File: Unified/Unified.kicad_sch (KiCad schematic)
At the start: 56 parts, among them J1 USB_C_Receptacle_USB2.0_16P, J10 JST_switch_1, J11 JST_switch_2, J12 Conn_touch_1, J13 Conn_touch_2, J14 Bat_pos_sel, J15 Bat_neg_sel, J16 JST_header, J2 JST_battery, J3 JST_header, J4 JST_speaker, J5 JST_debug_swd, J6 JST_debug_serial, J7 Conn_speaker_sd, J8 Conn_speaker_gain, J9 Conn_speaker_gnd, Q1 AO3401A, Q2 AO3400A, SW1 SW_power, U1 MCP73831-2-OT, U2 MAX98357A

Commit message: Add LEDs to unified PCB, currently routing
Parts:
- removed J16: JST_header, Connector_JST:JST_SH_BM04B-SRSS-TB_1x04-1MP_P1.00mm_Vertical, symbol Connector_Generic:Conn_01x04
- renumbered D9 to D10, D10 to D11, D11 to D12, D12 to D13, D13 to D14, D14 to D15, D15 to D16, D16 to D9
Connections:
- no-connect marks 4 -> 3
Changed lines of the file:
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@@
 		(at 29.21 67.31)
 	)
-	(no_connect
-		(at 33.02 199.39)
-	)
 	(wire
 		(pts
@@
 	(wire
 		(pts
-			(xy 33.02 191.77) (xy 36.83 191.77)
-		)
-		(stroke
-			(width 0)
-			(type default)
-		)
-	)
-	(wire
-		(pts
 			(xy 167.64 113.03) (xy 167.64 116.84)
 		)
@@
 	(wire
 		(pts
-			(xy 33.02 196.85) (xy 36.83 196.85)
-		)
-		(stroke
-			(width 0)
-			(type default)
-		)
-	)
-	(wire
-		(pts
 			(xy 311.15 132.08) (xy 317.5 132.08)
 		)
@@
 	(wire
 		(pts
-			(xy 33.02 199.39) (xy 36.83 199.39)
-		)
-		(stroke
-			(width 0)
-			(type default)
-		)
-	)
-	(wire
-		(pts
 			(xy 142.24 35.56) (xy 142.24 45.72)
 		)
@@
 	(wire
 		(pts
-			(xy 33.02 194.31) (xy 36.83 194.31)
-		)
-		(stroke
-			(width 0)
-			(type default)
-		)
-	)
-	(wire
-		(pts
 			(xy 99.06 168.91) (xy 102.87 168.91)
 		)
@@
 		)
 	)
-	(label "BAT_-"
-		(at 33.02 194.31 180)
-		(effects
-			(font
-				(size 1.27 1.27)
-			)
-			(justify right bottom)
-		)
-	)
 	(label "SPEAKER_LRC"
 		(at 90.17 152.4 180)
@@
 		)
 	)
-	(label "WS2812B_VS"
-		(at 33.02 191.77 180)
-		(effects
-			(font
-				(size 1.27 1.27)
-			)
-			(justify right bottom)
-		)
-	)
 	(label "SPEAKER_+"
 		(at 242.57 19.05 180)
@@
 		)
 	)
-	(label "WS2812B_DIN"
-		(at 33.02 196.85 180)
-		(effects
-			(font
-				(size 1.27 1.27)
-			)
-			(justify right bottom)
-		)
-	)
 	(symbol
 		(lib_id "LED:WS2812B")
@@
 		(dnp no)
 		(fields_autoplaced yes)
-		(property "Reference" "D14"
+		(property "Reference" "D15"
 			(at 212.09 223.4498 0)
 			(show_name no)
@@
 			(project "Unified"
 				(path "/86209ff5-e3e5-4edf-9087-a19295ca511e"
-					(reference "D14")
+					(reference "D15")
 					(unit 1)
 				)
@@
 		(dnp no)
 		(fields_autoplaced yes)
-		(property "Reference" "D15"
+		(property "Reference" "D16"
 			(at 237.49 223.4498 0)
 			(show_name no)
@@
 			(project "Unified"
 				(path "/86209ff5-e3e5-4edf-9087-a19295ca511e"
-					(reference "D15")
+					(reference "D16")
 					(unit 1)
 				)
@@
 		(dnp no)
 		(fields_autoplaced yes)
-		(property "Reference" "D13"
+		(property "Reference" "D14"
 			(at 186.69 223.4498 0)
 			(show_name no)
@@
 			(project "Unified"
 				(path "/86209ff5-e3e5-4edf-9087-a19295ca511e"
-					(reference "D13")
+					(reference "D14")
 					(unit 1)
 				)
@@
 	)
 	(symbol
-		(lib_id "Connector_Generic:Conn_01x04")
-		(at 41.91 194.31 0)
-		(unit 1)
-		(body_style 1)
-		(exclude_from_sim no)
-		(in_bom yes)
-		(on_board yes)
-		(in_pos_files yes)
-		(dnp no)
-		(property "Reference" "J16"
-			(at 45.212 192.532 0)
-			(show_name no)
-			(do_not_autoplace no)
-			(effects
-				(font
-					(size 1.27 1.27)
-				)
-			)
-		)
-		(property "Value" "JST_header"
-			(at 49.53 194.564 0)
-			(show_name no)
-			(do_not_autoplace no)
-			(effects
-				(font
-					(size 1.27 1.27)
-				)
-			)
-		)
-		(property "Footprint" "Connector_JST:JST_SH_BM04B-SRSS-TB_1x04-1MP_P1.00mm_Vertical"
-			(at 41.91 194.31 0)
-			(hide yes)
-			(show_name no)
-			(do_not_autoplace no)
-			(effects
-				(font
-					(size 1.27 1.27)
-				)
-			)
-		)
-		(property "Datasheet" ""
-			(at 41.91 194.31 0)
-			(hide yes)
-			(show_name no)
-			(do_not_autoplace no)
-			(effects
-				(font
-					(size 1.27 1.27)
-				)
-			)
-		)
-		(property "Description" "Generic connector, single row, 01x04, script generated (kicad-library-utils/schlib/autogen/connector/)"
-			(at 41.91 194.31 0)
-			(hide yes)
-			(show_name no)
-			(do_not_autoplace no)
-			(effects
-				(font
-					(size 1.27 1.27)
-				)
-			)
-		)
-		(pin "3"
-		)
-		(pin "1"
-		)
-		(pin "2"
-		)
-		(pin "4"
-		)
-		(instances
-			(project "Unified"
-				(path "/86209ff5-e3e5-4edf-9087-a19295ca511e"
-					(reference "J16")
-					(unit 1)
-				)
-			)
-		)
-	)
-	(symbol
 		(lib_id "LED:WS2812B")
 		(at 72.39 229.87 0)
@@
 		(dnp no)
 		(fields_autoplaced yes)
-		(property "Reference" "D9"
+		(property "Reference" "D10"
 			(at 83.82 223.4498 0)
 			(show_name no)
@@
 			(project "Unified"
 				(path "/86209ff5-e3e5-4edf-9087-a19295ca511e"
-					(reference "D9")
+					(reference "D10")
 					(unit 1)
 				)
@@
 		(dnp no)
 		(fields_autoplaced yes)
-		(property "Reference" "D16"
+		(property "Reference" "D9"
 			(at 262.89 192.9698 0)
 			(show_name no)
@@
 			(project "Unified"
 				(path "/86209ff5-e3e5-4edf-9087-a19295ca511e"
-					(reference "D16")
+					(reference "D9")
 					(unit 1)
 				)
@@
 		(dnp no)
 		(fields_autoplaced yes)
-		(property "Reference" "D11"
+		(property "Reference" "D12"
 			(at 135.89 223.4498 0)
 			(show_name no)
@@
 			(project "Unified"
 				(path "/86209ff5-e3e5-4edf-9087-a19295ca511e"
-					(reference "D11")
+					(reference "D12")
 					(unit 1)
 				)
@@
 		(dnp no)
 		(fields_autoplaced yes)
-		(property "Reference" "D10"
+		(property "Reference" "D11"
 			(at 110.49 223.4498 0)
 			(show_name no)
@@
 			(project "Unified"
 				(path "/86209ff5-e3e5-4edf-9087-a19295ca511e"
-					(reference "D10")
+					(reference "D11")
 					(unit 1)
 				)
@@
 		(dnp no)
 		(fields_autoplaced yes)
-		(property "Reference" "D12"
+		(property "Reference" "D13"
 			(at 161.29 223.4498 0)
 			(show_name no)
@@
 			(project "Unified"
 				(path "/86209ff5-e3e5-4edf-9087-a19295ca511e"
-					(reference "D12")
+					(reference "D13")
 					(unit 1)
 				)

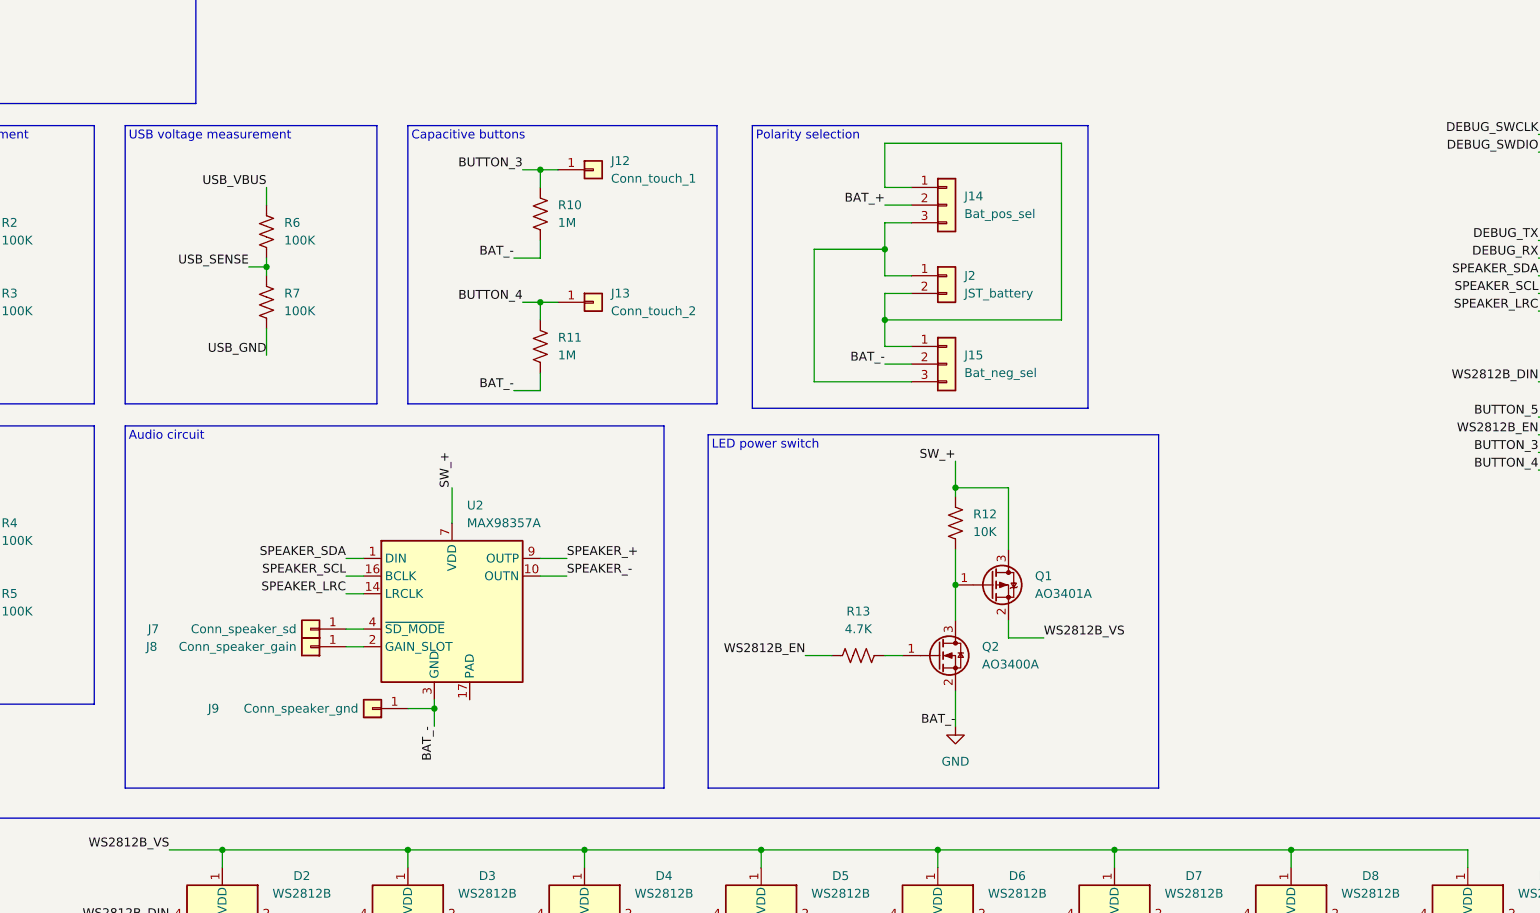
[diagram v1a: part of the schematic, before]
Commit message: Re-arrange for pin header for speaker
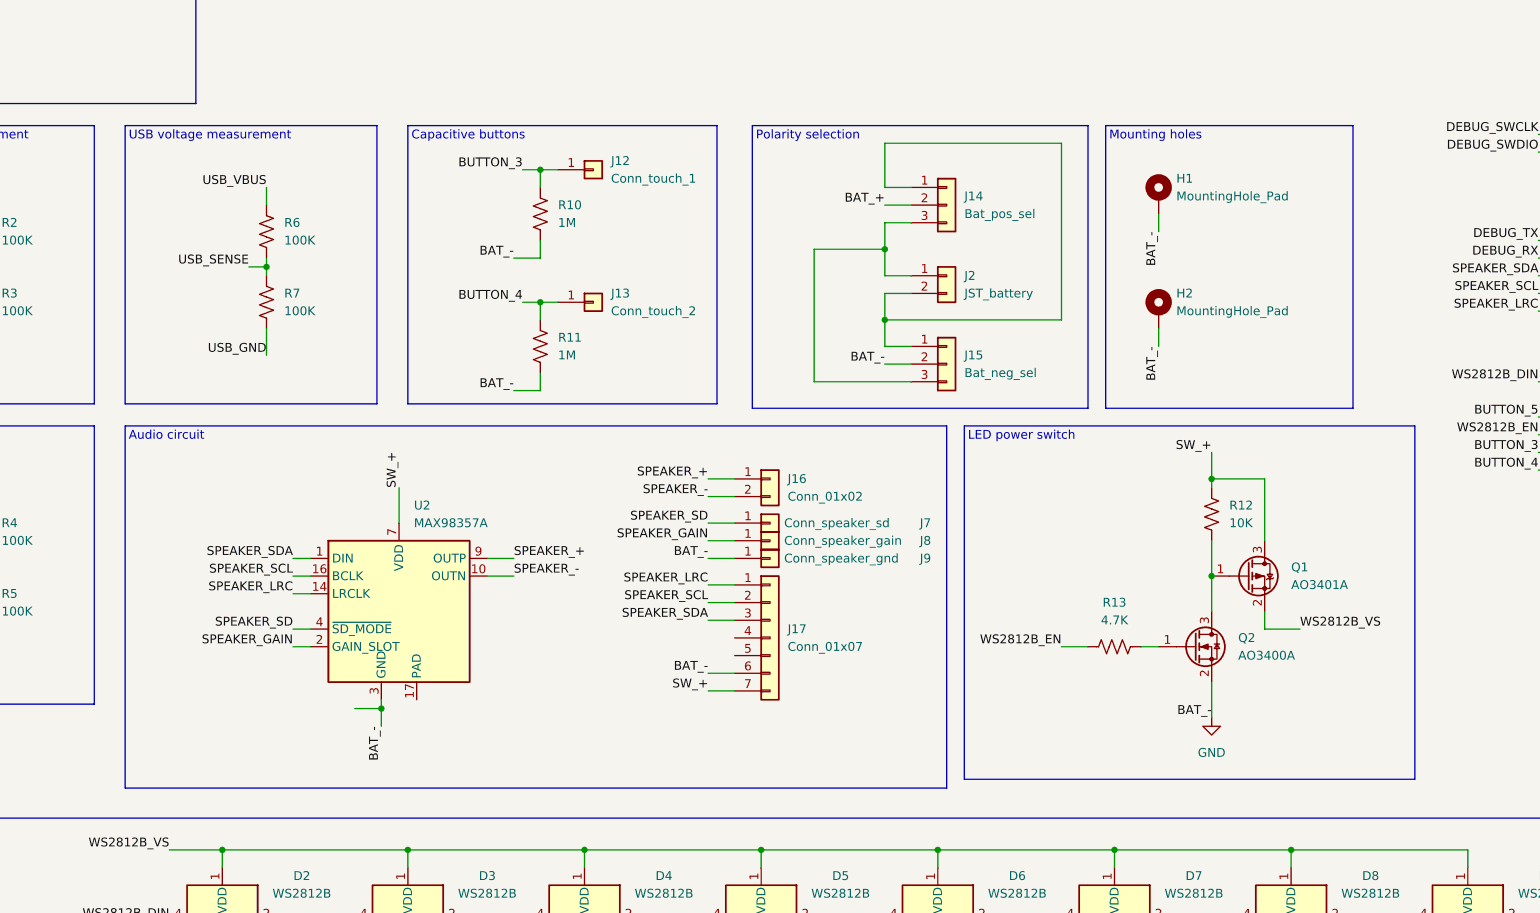
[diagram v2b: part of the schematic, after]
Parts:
- added H1, H2: MountingHole_Pad, MountingHole:MountingHole_4.3mm_M4_ISO7380_Pad, symbol Mechanical:MountingHole_Pad
- added J16: Conn_01x02, Connector_PinHeader_2.54mm:PinHeader_1x02_P2.54mm_Vertical, symbol Connector_Generic:Conn_01x02
- added J17: Conn_01x07, Connector_PinSocket_2.54mm:PinSocket_1x07_P2.54mm_Vertical, symbol Connector_Generic:Conn_01x07
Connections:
- net GND: now also H1.1, H2.1, J17.6 (Pin_6)
- net SPEAKER_+: now also J16.1 (Pin_1)
- net SPEAKER_-: now also J16.2 (Pin_2)
- net SPEAKER_LRC: now also J17.1 (Pin_1)
- net SPEAKER_SCL: now also J17.2 (Pin_2)
- net SPEAKER_SDA: now also J17.3 (Pin_3)
- net SW_+: now also J17.7 (Pin_7)
- net SPEAKER_GAIN: now reaches J8.1 (Pin_1), U2.2 (GAIN_SLOT)
- net SPEAKER_SD: now reaches J7.1 (Pin_1), U2.4 (~{SD_MODE})
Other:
- note added: "Mounting holes"
- moved on the sheet: Q1, Q2, R12, R13, U2

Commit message: Finalize routing, bump to V5
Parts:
- H1, H2: footprint MountingHole:MountingHole_4.3mm_M4_ISO7380_Pad -> MountingHole:MountingHole_2.2mm_M2_ISO7380_Pad
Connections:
- no-connect marks 3 -> 5
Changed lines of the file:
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@@
 	(paper "USLedger")
 	(title_block
-		(rev "V4")
+		(rev "V5")
 	)
 	(rectangle
@@
 	)
 	(junction
-		(at 95.25 168.91)
-		(diameter 0)
-		(color 0 0 0 0)
-	)
-	(junction
 		(at 99.06 219.71)
 		(diameter 0)
@@
 	)
 	(no_connect
+		(at 146.05 158.75)
+	)
+	(no_connect
 		(at 29.21 67.31)
 	)
+	(no_connect
+		(at 146.05 161.29)
+	)
 	(wire
 		(pts
@@
 	(wire
 		(pts
-			(xy 95.25 167.64) (xy 95.25 168.91)
-		)
-		(stroke
-			(width 0)
-			(type default)
-		)
-	)
-	(wire
-		(pts
 			(xy 200.66 189.23) (xy 226.06 189.23)
 		)
@@
 	(wire
 		(pts
-			(xy 95.25 168.91) (xy 95.25 171.45)
+			(xy 95.25 167.64) (xy 95.25 171.45)
 		)
 		(stroke
@@
 	(wire
 		(pts
-			(xy 91.44 168.91) (xy 95.25 168.91)
-		)
-		(stroke
-			(width 0)
-			(type default)
-		)
-	)
-	(wire
-		(pts
 			(xy 261.62 88.9) (xy 265.43 88.9)
 		)
@@
 			)
 		)
-		(property "Footprint" "MountingHole:MountingHole_4.3mm_M4_ISO7380_Pad"
+		(property "Footprint" "MountingHole:MountingHole_2.2mm_M2_ISO7380_Pad"
 			(at 207.01 95.25 0)
 			(hide yes)
@@
 			)
 		)
-		(property "Footprint" "MountingHole:MountingHole_4.3mm_M4_ISO7380_Pad"
+		(property "Footprint" "MountingHole:MountingHole_2.2mm_M2_ISO7380_Pad"
 			(at 207.01 111.76 0)
 			(hide yes)

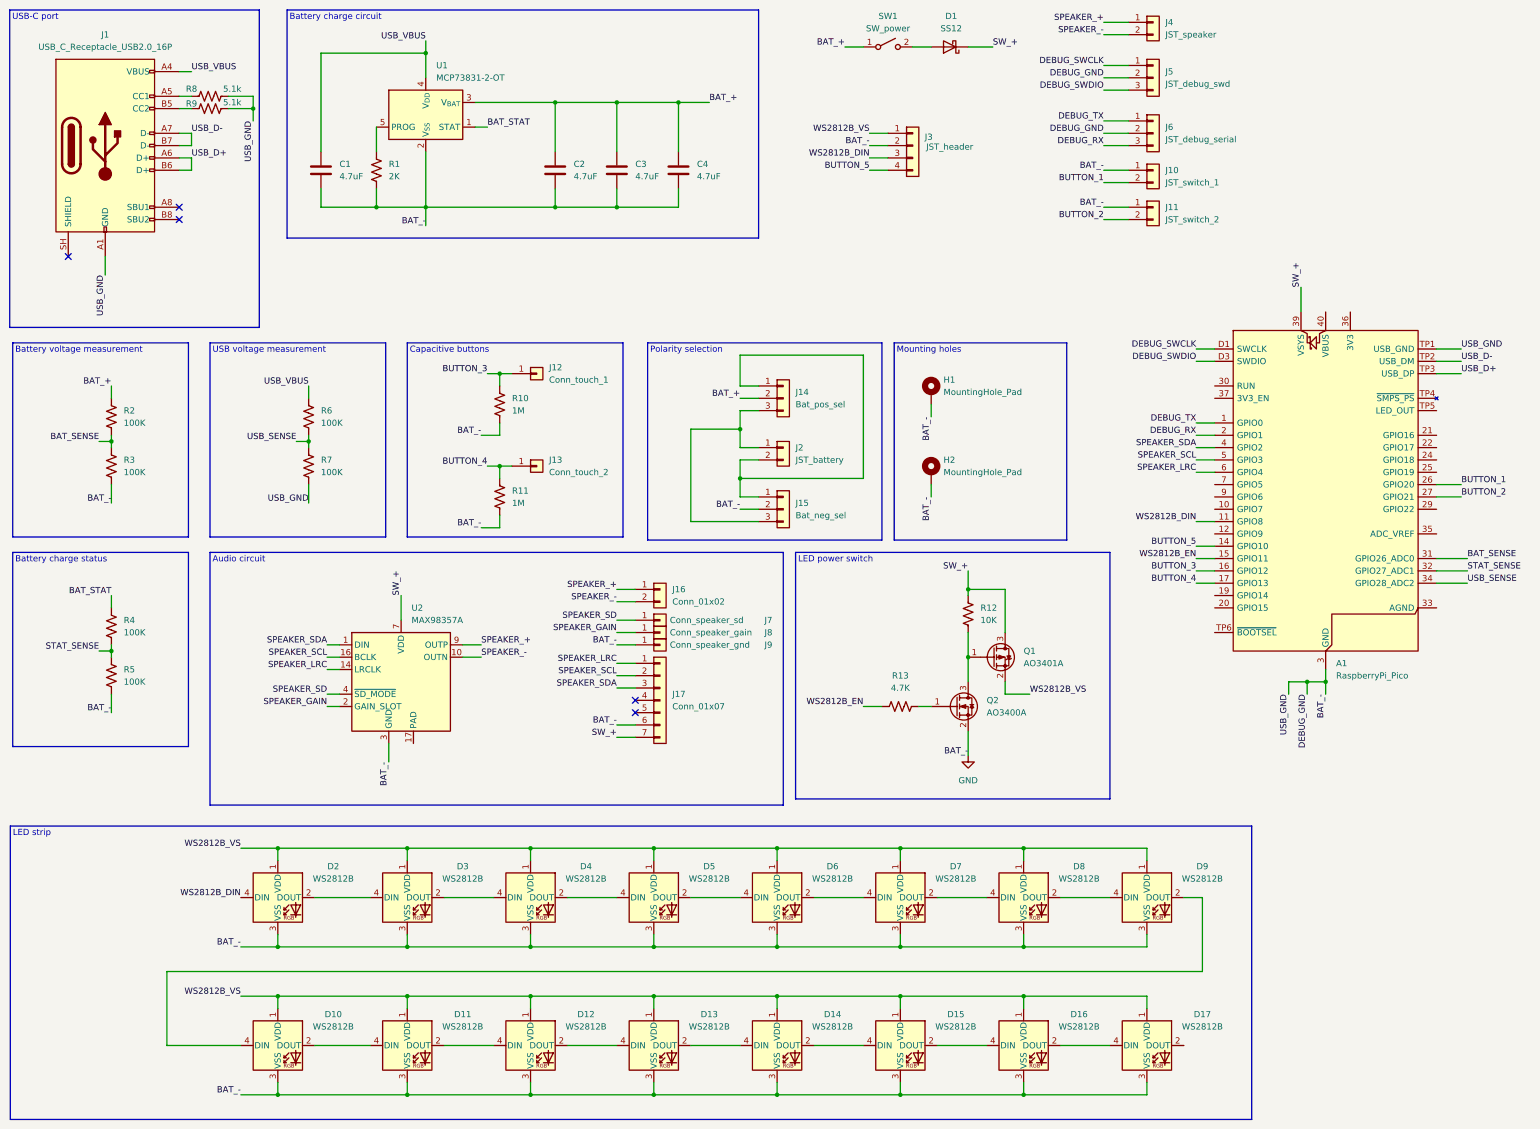
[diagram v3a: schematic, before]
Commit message: Add 100k resistor for defaulting audio chip gain to 15dB
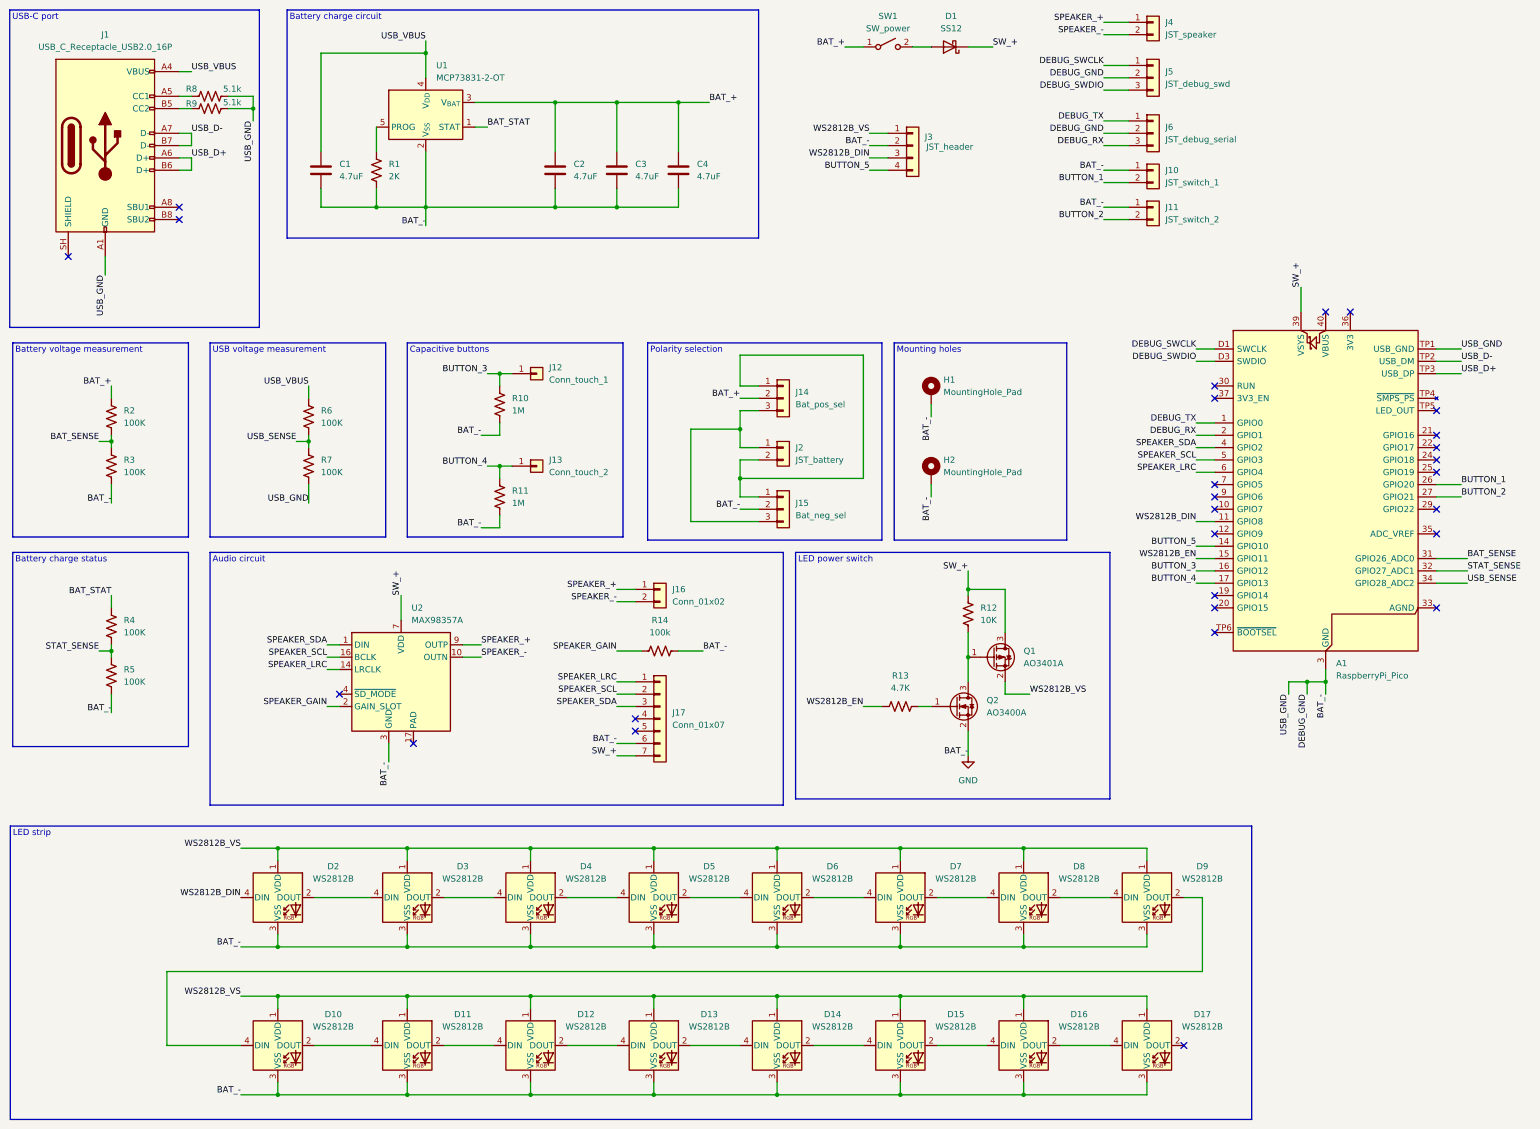
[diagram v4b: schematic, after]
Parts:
- removed J7: Conn_speaker_sd, TestPoint:TestPoint_THTPad_1.0x1.0mm_Drill0.5mm, symbol Connector_Generic:Conn_01x01
- removed J8: Conn_speaker_gain, TestPoint:TestPoint_THTPad_1.0x1.0mm_Drill0.5mm, symbol Connector_Generic:Conn_01x01
- removed J9: Conn_speaker_gnd, TestPoint:TestPoint_THTPad_1.0x1.0mm_Drill0.5mm, symbol Connector_Generic:Conn_01x01
- added R14: 100k, Resistor_SMD:R_0603_1608Metric_Pad0.98x0.95mm_HandSolder, symbol Device:R_US
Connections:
- net GND: now also R14.2
- net SPEAKER_GAIN: now also R14.1
- net SPEAKER_SD: no longer names the net of U2.4 (~{SD_MODE})
- no-connect marks 5 -> 27
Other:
- moved on the sheet: J17
